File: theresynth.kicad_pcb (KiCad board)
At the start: 2 copper layers, 216 x 69.7 mm, 133 parts, among them J1 Jack-12V AC, J2 AudioJack2, J3 AudioJack2, J4 AudioJack2, J5 AudioJack2, Q1 2N3904, Q2 2N3904, Q3 2N3904, Q4 2N3904, Q5 2N3904, Q6 J111, Q7 2N3904, U1 TL074, U2 LM78L12_TO92, U3 LM79L12_TO92, U4 TL074, U5 TL072

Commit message: completely connected
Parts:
- removed the C38 at (91.3, 100.5)
- removed the D6 at (130.0, 125.5)
- removed the R40 at (77.3, 95.3)
- removed the R42 at (69.7, 90.2)
- removed the R48 at (90.1, 97.7)
- removed the R50 at (90.1, 87.7)
- removed R52, R53: 10k, Resistor_THT:R_Axial_DIN0204_L3.6mm_D1.6mm_P7.62mm_Horizontal
- removed R55: 1k, Resistor_THT:R_Axial_DIN0204_L3.6mm_D1.6mm_P7.62mm_Horizontal
- removed the RV6 at (114.4, 125.5)
- removed the U5 at (90.1, 107.3)
- added ?: , MountingHole:MountingHole_3mm, F.Cu at (48.0, 63.8)
- added ?: , MountingHole:MountingHole_3mm, F.Cu at (254.0, 63.8)
- added ?: , MountingHole:MountingHole_3mm, F.Cu at (254.0, 125.5)
- added ?: , MountingHole:MountingHole_3mm, F.Cu at (48.0, 125.5)
- added C19: 100n, Capacitor_THT:C_Rect_L7.2mm_W2.5mm_P5.00mm_FKS2_FKP2_MKS2_MKP2, F.Cu at (137.4, 95.4)
- added C20: 100n, Capacitor_THT:C_Rect_L7.2mm_W2.5mm_P5.00mm_FKS2_FKP2_MKS2_MKP2, F.Cu at (152.9, 95.4)
- added C39: 100n, Capacitor_THT:C_Rect_L7.2mm_W2.5mm_P5.00mm_FKS2_FKP2_MKS2_MKP2, F.Cu at (78.2, 95.3)
- added C40: 100n, Capacitor_THT:C_Rect_L7.2mm_W2.5mm_P5.00mm_FKS2_FKP2_MKS2_MKP2, F.Cu at (93.6, 94.9)
- added C42: 100n, Capacitor_THT:C_Rect_L7.2mm_W2.5mm_P5.00mm_FKS2_FKP2_MKS2_MKP2, F.Cu at (176.6, 71.0)
- added C43: 100n, Capacitor_THT:C_Rect_L7.2mm_W2.5mm_P5.00mm_FKS2_FKP2_MKS2_MKP2, F.Cu at (192.6, 71.1)
- added D1: LED, LED_THT:LED_D3.0mm, F.Cu at (152.2, 125.8)
- added D7: LED, LED_THT:LED_D3.0mm, F.Cu at (54.2, 125.8)
- added R32: 1k, Resistor_THT:R_Axial_DIN0204_L3.6mm_D1.6mm_P7.62mm_Horizontal, F.Cu at (198.8, 76.2)
- added R34: 5k, Resistor_THT:R_Axial_DIN0204_L3.6mm_D1.6mm_P7.62mm_Horizontal, F.Cu at (198.9, 66.0)
- added R35: 10k, Resistor_THT:R_Axial_DIN0204_L3.6mm_D1.6mm_P7.62mm_Horizontal, F.Cu at (191.3, 63.5)
- added RV4: 100k, Potentiometer_THT:Potentiometer_Bourns_3296W_Vertical, F.Cu at (160.3, 68.3)
- added RV7: 100k, Potentiometer_THT:Potentiometer_Alps_RK163_Single_Horizontal, F.Cu at (72.1, 125.2)
- added SW1: SW_SPST, Eurorack:Horizontal_SPDT_2MS5T2B2M7RE, F.Cu at (61.5, 120.8)
- added U2: TL074, Package_DIP:DIP-14_W7.62mm_LongPads, F.Cu at (180.8, 63.5)
- C3: footprint Capacitor_THT:C_Rect_L7.0mm_W6.5mm_P5.00mm -> Eurorack:Variable_Capacitor_W6.5mm_P5.00mm
- C31: renamed from C29; footprint Capacitor_THT:C_Rect_L7.0mm_W6.5mm_P5.00mm -> Eurorack:Variable_Capacitor_W6.5mm_P5.00mm
- C38: renamed from C36; value 33n -> 100n
- J5: value AudioJack2 -> External Ground; footprint Eurorack:PJ302M -> Connector_Pin:Pin_D1.4mm_L8.5mm_W2.8mm_FlatFork
- R44: renamed from R45; value 100k -> 220k
- R47: renamed from R43; value 100k -> 5k
- R48: renamed from R44; value 100k -> 10k
- R51: value 10k -> 1k
- RV3: value R_POT -> 100k
- RV5: renamed from RV4; footprint Potentiometer_THT:Potentiometer_Alps_RK163_Single_Horizontal -> Potentiometer_THT:Potentiometer_Bourns_3296W_Vertical
- moved R49 83.8 mm to (170.5, 63.5)
- moved R50 76.8 mm to (170.5, 78.8), turned to 0 degrees
- moved R51 67.1 mm to (56.7, 120.2)
- moved R33 38.0 mm to (191.3, 68.5)
- moved R37 36.8 mm to (170.5, 76.2)
- moved J2 33.7 mm to (211.6, 67.7)
- moved R24 32.4 mm to (100.1, 90.1)
- moved R48 30.7 mm to (100.1, 92.3), turned to 180 degrees
- moved R36 20.9 mm to (198.8, 78.8)
- moved RV5 19.7 mm to (78.1, 107.0), turned to 0 degrees
- moved D6 13.4 mm to (119.5, 125.8)
- moved R47 10.8 mm to (92.4, 100.8)
- moved J1 8.21 mm to (80.2, 73.8)
- moved R23 7.90 mm to (151.8, 87.4)
- moved RV6 7.75 mm to (97.8, 125.2)
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- renumbered C19 to C21, C20 to C22, C25 to C23, C21 to C24, C22 to C25, C23 to C26, C24 to C27, C26 to C28, C27 to C29, C28 to C30, C30 to C32, C31 to C33, C32 to C34, C33 to C35, C34 to C36, C35 to C37, C37 to C41, D1 to D2, D2 to D3, D3 to D4, D4 to D5, D5 to D6, J3 to J2, J2 to J3, R30 to R27, R27 to R28, R28 to R29, R29 to R30, R32 to R33, R34 to R36, R33 to R37, R35 to R38, R36 to R39, R37 to R40, R38 to R41, R39 to R42, R41 to R43, R46 to R45, R47 to R46, R54 to R49, R49 to R50, RV5 to RV6, U2 to U3, U3 to U4, U4 to U5
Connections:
- C23 pad 1: Net-(C25-Pad1) -> Net-(C23-Pad1)
- C28 pad 1: Net-(C26-Pad1) (its old number) -> Net-(C28-Pad1)
- C41 pad 1: Net-(C37-Pad1) (its old number) -> Net-(C41-Pad1)
- D2 pad 2: Net-(D1-Pad2) -> Net-(D2-Pad2)
- D3 pad 1: Net-(D1-Pad2) -> Net-(D2-Pad2)
- D4 pad 1: Net-(C25-Pad1) -> Net-(C23-Pad1)
- J1 pad 1: Net-(D1-Pad2) -> Net-(J1-Pad1)
- J4 pad T: VolumeControlOut -> Net-(J4-PadT)
- R33 pad 1: Net-(C25-Pad1) -> Net-(C23-Pad1)
- R36 pad 2: Net-(C26-Pad1) (its old number) -> Net-(C28-Pad1)
- R37 pad 2: Net-(C25-Pad1) -> Net-(R35-Pad1)
- R43 pad 1: Net-(R41-Pad1) -> Net-(R43-Pad1)
- R46 pad 1: Net-(C38-Pad2) -> Net-(C41-Pad1)
- R47 pad 1: Net-(R41-Pad1) -> Net-(R47-Pad1)
- R48 pad 1: Net-(R40-Pad2) -> Net-(R47-Pad1)
- R48 pad 2: Net-(R44-Pad2) -> Net-(R48-Pad2)
- R50 pad 1: VolumeControlOut -> Net-(J4-PadT)
- R50 pad 2: Net-(C38-Pad1) (its old number) -> Net-(R50-Pad2)
- R51 pad 1: Net-(J5-PadT) -> Net-(D7-Pad2)
- R51 pad 2: Net-(R50-Pad1) -> +12V
- RV5 pad 1: +12V -> -12V
- RV5 pad 2: Net-(R42-Pad2) -> Net-(R43-Pad1)
- RV5 pad 3: GND -> +12V
- U1 pad 12: Net-(R26-Pad1) -> Net-(C28-Pad1)
- U1 pad 8: Net-(C26-Pad1) (its old number) -> Net-(C28-Pad1)
- U1 pad 9: Net-(C26-Pad1) (its old number) -> Net-(C28-Pad1)
- U5 pad 10: Net-(C37-Pad1) (its old number) -> Net-(C41-Pad1)
- U5 pad 12: Net-(C38-Pad1) (its old number) -> Net-(R48-Pad2)
- U5 pad 13: Net-(RV6-Pad2) -> VolumeControlOut
- U5 pad 14: Net-(R50-Pad1) -> VolumeControlOut
- U5 pad 2: Net-(R40-Pad2) -> Net-(R44-Pad2)
- U5 pad 3: Net-(R41-Pad1) -> Net-(R43-Pad1)
- U5 pad 8: Net-(C38-Pad1) (its old number) -> Net-(R48-Pad2)
- U5 pad 9: Net-(C38-Pad1) (its old number) -> Net-(R47-Pad1)
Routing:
- net +12V: track 58.8 -> 411.7 mm
- net -12V: track 0.00 -> 287.9 mm
- net Net-(R48-Pad2): track 0.00 -> 119.8 mm
- net Net-(D1-Pad1): track 0.00 -> 99.2 mm
- net Net-(D6-Pad1): track 0.00 -> 95.1 mm
- net Net-(D2-Pad2): track 0.00 -> 71.3 mm
- net Net-(C28-Pad1): track 0.00 -> 69.7 mm
- net Net-(R21-Pad1): track 0.00 -> 65.3 mm
- net Net-(J1-Pad1): track 0.00 -> 60.9 mm
- net Net-(C13-Pad2): track 11.0 -> 66.7 mm
- net Net-(C21-Pad2): track 0.00 -> 53.3 mm
- net Net-(C23-Pad1): track 0.00 -> 53.2 mm
- net Net-(C37-Pad1): track 16.1 -> 65.6 mm
- net Net-(C41-Pad1): track 0.00 -> 49.1 mm
- net Net-(Q5-Pad2): track 7.81 -> 56.8 mm
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- added copper zone on B.Cu, net GND
- added copper zone on F.Cu, net GND
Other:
- board size 216 x 69.7 mm -> 214 x 69.7 mm
- net class Power added: clearance 0.4, trace_width 0.5, via_dia 0.8, via_drill 0.4
- board text added: "Audio Filter"
- board text added: "External Ground"
- board text added: "Fine CV1 Offset"
- board text added: "On/Off"
- board text added: "Pitch Antenna"
- board text added: "Theresynth © 2020 Marco Martin"
- board text added: "V1.0"
- board text added: "Volume Antenna"
- board text added: "Volume CV Offset and Amplifier"
- board text added: "Volume Oscillator"
- board text removed: "Gate Threshold"
- board text removed: "Gate1"

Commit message: add phones output
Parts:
- added J6: AudioJack3_Switch, Connector_Audio:Jack_3.5mm_Ledino_KB3SPRS_Horizontal, F.Cu at (58.8, 153.1)
- added R52: 1k, Resistor_THT:R_Axial_DIN0204_L3.6mm_D1.6mm_P7.62mm_Horizontal, F.Cu at (50.0, 142.7)
- added RV8: 100k, Potentiometer_THT:Potentiometer_Alps_RK163_Single_Horizontal, F.Cu at (25.2, 151.9)
- C24, C25: value 2200u -> 4700u
- C32: value 22p -> 47p
- J5: value External Ground -> Ext. GND
- U3: value LM78L12_TO92 -> LM7812_TO220; footprint Package_TO_SOT_THT:TO-92_Inline_Wide -> Package_TO_SOT_THT:TO-220-3_Vertical
- U4: value LM79L12_TO92 -> LM7912_TO220; footprint Package_TO_SOT_THT:TO-92_Inline_Wide -> Package_TO_SOT_THT:TO-220-3_Vertical
- moved D4 72.9 mm to (215.8, 65.1), turned to 180 degrees
- moved C23 67.3 mm to (213.3, 69.9), turned to 180 degrees
- moved R27 53.2 mm to (205.8, 65.1), turned to 180 degrees
- moved J3 50.6 mm to (186.9, 67.7)
- moved C30 46.3 mm to (106.2, 81.6)
- moved C22 41.7 mm to (200.4, 68.0), turned to 0 degrees
- moved RV4 39.0 mm to (199.1, 72.5), turned to 180 degrees
- moved U3 33.8 mm to (120.8, 78.3)
- moved C29 31.0 mm to (127.2, 81.6), turned to 180 degrees
- moved D2 28.6 mm to (64.5, 82.0), turned to 90 degrees
- moved J5 27.1 mm to (85.2, 63.5)
- moved U4 26.9 mm to (104.8, 78.3)
- moved J1 23.7 mm to (56.5, 73.8)
- moved C42 21.5 mm to (155.1, 71.0)
- moved C43 21.5 mm to (171.1, 71.1)
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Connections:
- R48 pad 2: Net-(R48-Pad2) -> VolumeControlOut
- U1 pad 12: Net-(C28-Pad1) -> Net-(R23-Pad1)
- U2 pad 3: Net-(R48-Pad2) -> VolumeControlOut
- U2 pad 5: Net-(R48-Pad2) -> VolumeControlOut
- U3 pad 1: +12V -> Net-(C24-Pad1)
- U3 pad 3: Net-(C24-Pad1) -> +12V
- U5 pad 12: Net-(R48-Pad2) -> Net-(C28-Pad1)
- U5 pad 13: VolumeControlOut -> Net-(R52-Pad2)
- U5 pad 14: VolumeControlOut -> Net-(R52-Pad2)
- U5 pad 8: Net-(R48-Pad2) -> VolumeControlOut
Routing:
- net -12V: track 287.9 -> 122.6 mm
- net +12V: track 411.7 -> 281.6 mm
- net Net-(R48-Pad2): track 119.8 -> 0.00 mm
- net Net-(D2-Pad2): track 71.3 -> 0.00 mm
- net VolumeControlOut: track 5.26 -> 68.7 mm
- net Net-(J1-Pad1): track 60.9 -> 0.00 mm
- net Net-(J4-PadT): track 47.8 -> 0.00 mm
- net Net-(D6-Pad1): track 95.1 -> 57.0 mm
- net Net-(J3-PadT): track 36.5 -> 0.00 mm
- net Net-(J2-PadT): track 14.7 -> 50.9 mm
- net Net-(C25-Pad2): track 34.2 -> 0.00 mm
- net Net-(C23-Pad1): track 53.2 -> 21.5 mm
- net Net-(C28-Pad1): track 69.7 -> 41.4 mm
- net Net-(C24-Pad1): track 28.0 -> 0.00 mm
- net Net-(D1-Pad1): track 99.2 -> 119.9 mm
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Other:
- board text added: "Ext. GND"
- board text added: "TODO: un jack per parte, l'envelope va spostata tra i due CV"
- board text removed: "External Ground"

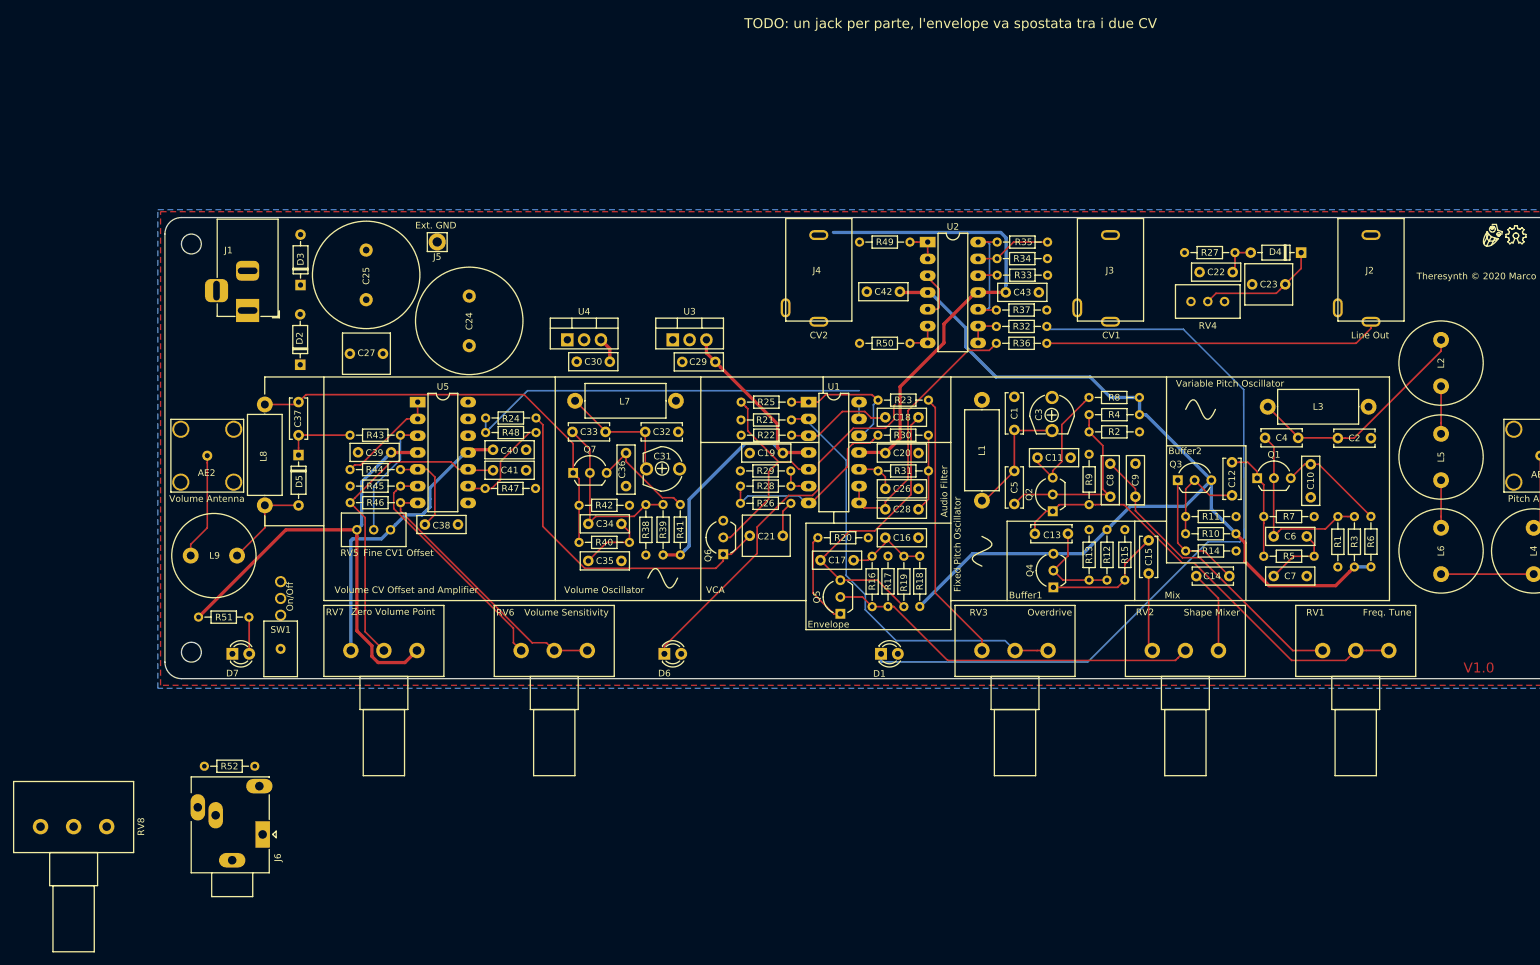
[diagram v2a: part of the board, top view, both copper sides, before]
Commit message: removed 2 opamp units
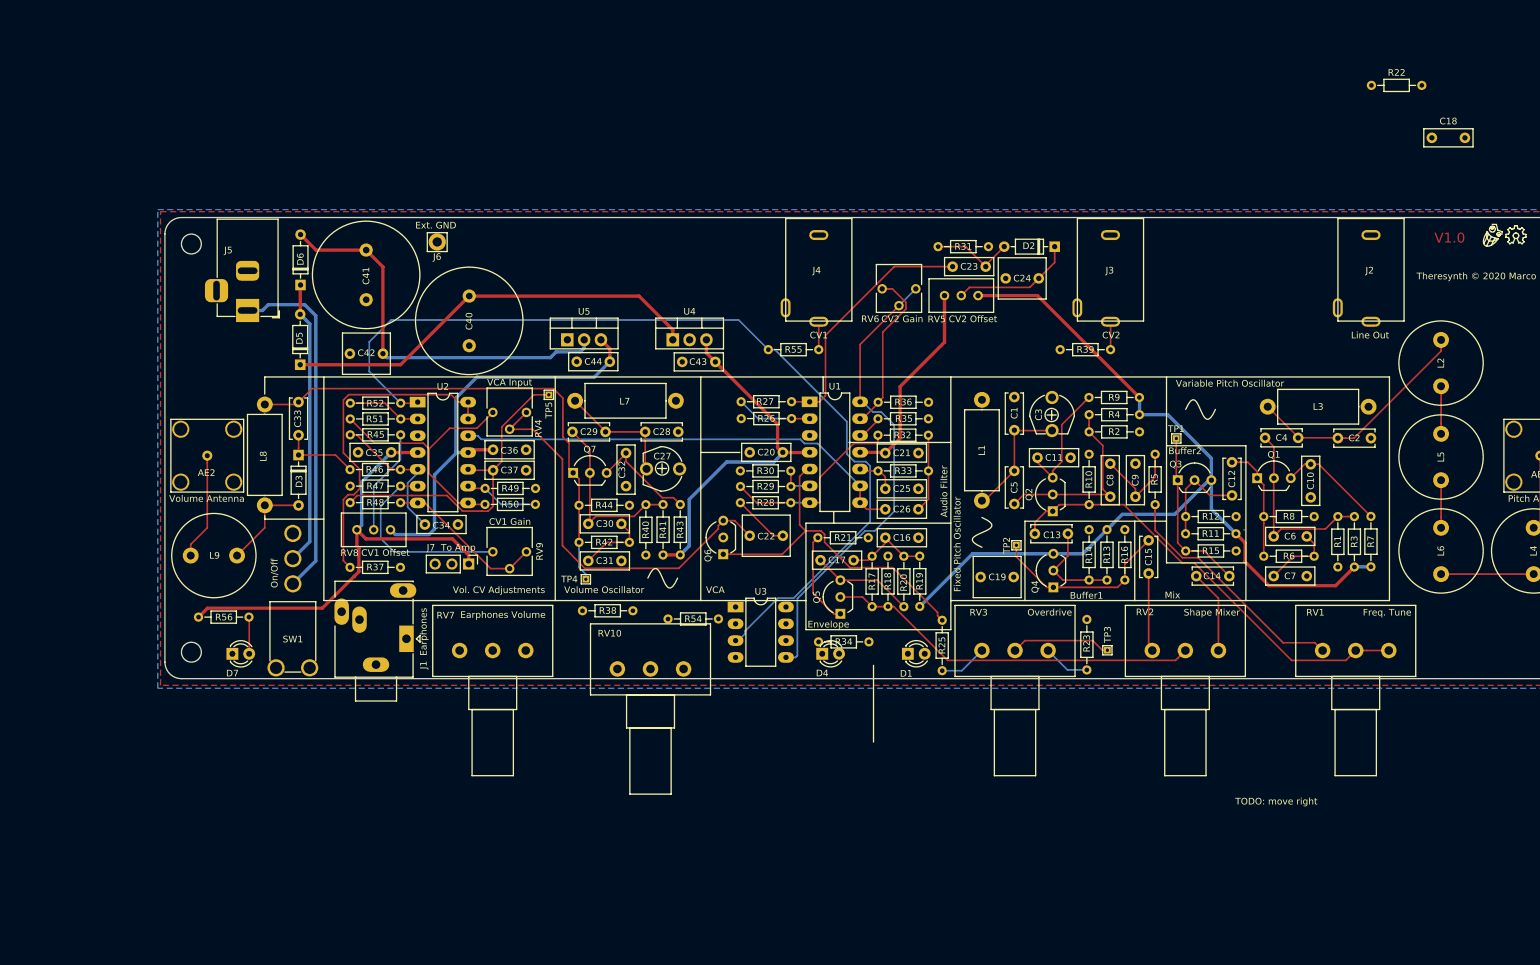
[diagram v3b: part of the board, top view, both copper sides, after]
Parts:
- removed the C42 at (155.1, 71.0)
- removed the C43 at (171.1, 71.1)
- removed the R23 at (151.8, 87.4)
- removed R24: 9.52k, Resistor_THT:R_Axial_DIN0204_L3.6mm_D1.6mm_P7.62mm_Horizontal
- removed the R43 at (79.6, 92.7)
- removed the RV7 at (72.1, 125.2)
- added C18: 10n, Capacitor_THT:C_Rect_L7.2mm_W2.5mm_P5.00mm_FKS2_FKP2_MKS2_MKP2, F.Cu at (235.5, 47.8)
- added J7: To_Amp, Connector_PinHeader_2.54mm:PinHeader_1x03_P2.54mm_Vertical, F.Cu at (89.9, 112.2)
- added R22: 2.2k, Resistor_THT:R_Axial_DIN0204_L3.6mm_D1.6mm_P7.62mm_Horizontal, F.Cu at (226.4, 39.8)
- added R45: 220k, Resistor_THT:R_Axial_DIN0204_L3.6mm_D1.6mm_P7.62mm_Horizontal, F.Cu at (72.0, 92.7)
- added R5: 220, Resistor_THT:R_Axial_DIN0204_L3.6mm_D1.6mm_P7.62mm_Horizontal, F.Cu at (193.7, 103.2)
- added R51: 10k, Resistor_THT:R_Axial_DIN0204_L3.6mm_D1.6mm_P7.62mm_Horizontal, F.Cu at (79.6, 90.2)
- added R52: 10k, Resistor_THT:R_Axial_DIN0204_L3.6mm_D1.6mm_P7.62mm_Horizontal, F.Cu at (72.0, 87.9)
- added RV10: 100k, Potentiometer_THT:Potentiometer_Alps_RK163_Single_Horizontal, F.Cu at (112.4, 128.0)
- added RV4: 10k, Potentiometer_THT:Potentiometer_Vishay_T73YP_Vertical, F.Cu at (93.6, 89.3)
- added RV6: 10k, Potentiometer_THT:Potentiometer_Vishay_T73YP_Vertical, F.Cu at (152.4, 70.6)
- added TP1: TestPoint, TestPoint:TestPoint_THTPad_1.0x1.0mm_Drill0.5mm, F.Cu at (196.9, 93.2)
- added TP2: TestPoint, TestPoint:TestPoint_THTPad_1.0x1.0mm_Drill0.5mm, F.Cu at (172.7, 109.3)
- added TP3: TestPoint, TestPoint:TestPoint_THTPad_1.0x1.0mm_Drill0.5mm, F.Cu at (186.5, 125.2)
- added TP4: TestPoint, TestPoint:TestPoint_THTPad_1.0x1.0mm_Drill0.5mm, F.Cu at (107.6, 114.5)
- added TP5: TestPoint, TestPoint:TestPoint_THTPad_1.0x1.0mm_Drill0.5mm, F.Cu at (102.0, 86.6)
- C1: value 33p -> 22p
- C19: renamed from C18; value 100n -> 1u; footprint Capacitor_THT:C_Rect_L7.2mm_W2.5mm_P5.00mm_FKS2_FKP2_MKS2_MKP2 -> Capacitor_THT:C_Rect_L7.0mm_W6.0mm_P5.00mm
- C2: value 47p -> 22p
- C23: renamed from C22; value 40n -> 10n
- C3: value 60p -> 20p
- Q6: value J111 -> J113
- R23: renamed from R21; value 1k -> 10k
- R26: renamed from R22; value 100k -> 10k
- R27: renamed from R35; value 10k -> 100k
- R31: renamed from R27; value 10k -> 100k
- R36: renamed from R34; value 5k -> 1k
- R49: renamed from R47; value 5k -> 10k
- RV9: renamed from RV6; footprint Potentiometer_THT:Potentiometer_Alps_RK163_Single_Horizontal -> Potentiometer_THT:Potentiometer_Vishay_T73YP_Vertical
- SW1: footprint Eurorack:Horizontal_SPDT_2MS5T2B2M7RE -> Eurorack:Horizontal_SPDT
- U3: renamed from U2; value TL074 -> TL072; footprint Package_DIP:DIP-14_W7.62mm_LongPads -> Package_DIP:DIP-8_W7.62mm_LongPads
- moved R38 74.5 mm to (114.7, 119.2)
- moved RV7 68.7 mm to (88.5, 125.2)
- moved R54 63.9 mm to (120.0, 120.5)
- moved U3 62.3 mm to (130.3, 118.7)
- moved R23 58.5 mm to (183.4, 128.2), turned to 90 degrees
- moved R34 54.7 mm to (150.4, 123.9)
- moved R25 44.8 mm to (161.5, 120.7), turned to 270 degrees
- moved R37 42.2 mm to (79.6, 112.7), turned to 180 degrees
- moved R27 39.3 mm to (138.7, 87.6), turned to 180 degrees
- moved C24 37.3 mm to (176.1, 69.0)
- moved D2 37.3 mm to (178.5, 64.2)
- moved R31 37.3 mm to (168.5, 64.2)
- moved RV5 37.3 mm to (161.8, 71.6)
- moved J1 36.7 mm to (80.5, 123.5)
- moved C23 32.3 mm to (168.1, 67.2), turned to 180 degrees
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- renumbered C19 to C20, C20 to C21, C21 to C22, C23 to C24, C26 to C25, C28 to C26, C31 to C27, C32 to C28, C33 to C29, C34 to C30, C35 to C31, C36 to C32, C37 to C33, C38 to C34, C39 to C35, C40 to C36, C41 to C37, C24 to C40, C25 to C41, C27 to C42, C29 to C43, C30 to C44, D4 to D2, D5 to D3, D6 to D4, D2 to D5, D3 to D6, J6 to J1, J1 to J5, J5 to J6, R9 to R10, R10 to R11, R11 to R12, R12 to R13, R13 to R14, R14 to R15, R15 to R16, R16 to R17, R17 to R18, R18 to R19, R19 to R20, R20 to R21, R26 to R28, R28 to R29, R29 to R30, R30 to R32, R31 to R33, R32 to R34, R33 to R35, R52 to R37, R36 to R38, R37 to R39, R38 to R40, R39 to R41, R40 to R42, R41 to R43, R42 to R44, R44 to R46, R45 to R47, R46 to R48, R48 to R50, R49 to R54, R50 to R55, R51 to R56, R5 to R6, R6 to R7, R7 to R8, R8 to R9, RV4 to RV5, RV8 to RV7, RV5 to RV8, U5 to U2, U3 to U4, U4 to U5
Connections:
- C19 pad 1: Net-(C18-Pad1) -> Net-(C19-Pad1)
- C19 pad 2: Net-(C17-Pad2) -> Net-(C18-Pad1)
- C22 pad 2: Net-(C21-Pad2) -> Net-(C22-Pad2)
- C23 pad 1: GND -> Net-(C23-Pad1)
- C23 pad 2: Net-(C22-Pad2) -> Net-(C23-Pad2)
- C24 pad 1: Net-(C23-Pad1) -> Net-(C24-Pad1)
- C33 pad 2: Net-(C37-Pad2) -> Net-(C33-Pad2)
- D2 pad 1: Net-(C23-Pad1) -> Net-(C24-Pad1)
- D2 pad 2: Net-(C22-Pad2) -> Net-(C23-Pad1)
- D3 pad 1: Net-(C37-Pad2) -> Net-(C33-Pad2)
- D4 pad 1: Net-(D6-Pad1) -> GND
- D4 pad 2: GND -> Net-(D4-Pad2)
- J1 pad TN: (no net) -> Net-(J1-PadTN)
- Q6 pad 1: Net-(C21-Pad2) -> Net-(Q6-Pad1)
- Q6 pad 2: Net-(Q6-Pad2) -> GND
- Q6 pad 3: GND -> Net-(C22-Pad2)
- R23 pad 1: Net-(R21-Pad1) -> Net-(R23-Pad1)
- R25 pad 1: Net-(Q6-Pad2) -> Net-(Q6-Pad1)
- R25 pad 2: Net-(R23-Pad1) -> Net-(R25-Pad2)
- R26 pad 2: Net-(C18-Pad1) -> Net-(R26-Pad2)
- R27 pad 1: Net-(R35-Pad1) -> Net-(C23-Pad2)
- R27 pad 2: Net-(R34-Pad2) -> Net-(R26-Pad2)
- R31 pad 1: Net-(C22-Pad2) -> GND
- R31 pad 2: Net-(R27-Pad2) -> Net-(C23-Pad1)
- R34 pad 2: Net-(R32-Pad2) -> Net-(R34-Pad2)
- R35 pad 1: Net-(C23-Pad1) -> Net-(C24-Pad1)
- R36 pad 2: Net-(R34-Pad2) -> Net-(R36-Pad2)
- R38 pad 1: Net-(J2-PadT) -> Net-(R38-Pad1)
- R39 pad 2: Net-(R35-Pad1) -> Net-(R39-Pad2)
- R46 pad 2: Net-(R44-Pad2) -> Net-(C33-Pad2)
- R54 pad 1: Net-(D6-Pad1) -> Net-(D4-Pad2)
- R55 pad 2: Net-(R50-Pad2) -> Net-(R52-Pad2)
- RV1 pad 1: Net-(C8-Pad2) -> Net-(R5-Pad1)
- RV3 pad 1: Net-(R23-Pad2) -> Net-(R25-Pad2)
- RV3 pad 2: Net-(R21-Pad1) -> Net-(C19-Pad1)
- RV3 pad 3: Net-(R21-Pad1) -> Net-(R23-Pad1)
- RV5 pad 2: Net-(C23-Pad1) -> Net-(C24-Pad1)
- RV8 pad 2: Net-(R43-Pad1) -> Net-(R45-Pad2)
- U1 pad 1: Net-(R23-Pad1) -> Net-(C23-Pad2)
- U1 pad 12: Net-(R23-Pad1) -> Net-(C24-Pad1)
- U1 pad 13: Net-(R27-Pad2) -> Net-(R36-Pad2)
- U1 pad 14: Net-(R27-Pad2) -> Net-(R39-Pad2)
- U1 pad 2: Net-(R21-Pad1) -> Net-(R26-Pad2)
- U1 pad 3: Net-(C18-Pad1) -> Net-(C19-Pad1)
- U1 pad 5: Net-(Q6-Pad2) -> Net-(Q6-Pad1)
- U2 pad 1: Net-(R44-Pad2) -> Net-(R52-Pad2)
- U2 pad 2: Net-(R44-Pad2) -> Net-(R51-Pad1)
- U2 pad 3: Net-(R43-Pad1) -> GND
- U3 pad 3: VolumeControlOut -> Net-(R52-Pad2)
- U3 pad 4: +12V -> -12V
- U3 pad 5: VolumeControlOut -> Net-(R39-Pad2)
- U3 pad 6: Net-(R50-Pad2) -> Net-(R34-Pad2)
- U3 pad 7: Net-(R50-Pad2) -> Net-(R34-Pad2)
- U3 pad 8: Net-(R32-Pad2) -> +12V
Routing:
- net Net-(R52-Pad2): track 0.00 -> 139.4 mm
- net Net-(D1-Pad1): track 119.9 -> 0.00 mm
- net Net-(R39-Pad2): track 0.00 -> 70.8 mm
- net Net-(R21-Pad1): track 65.3 -> 0.00 mm
- net Net-(C40-Pad1): track 0.00 -> 64.2 mm
- net Net-(C41-Pad2): track 0.00 -> 60.1 mm
- net Net-(D6-Pad1): track 57.0 -> 0.00 mm
- net Net-(C22-Pad2): track 5.47 -> 60.5 mm
- net Net-(C21-Pad2): track 53.3 -> 0.00 mm
- net Net-(J5-Pad1): track 0.00 -> 53.3 mm
- net Net-(Q6-Pad1): track 0.00 -> 51.7 mm
- net Net-(J2-PadT): track 50.9 -> 0.00 mm
- net Net-(R37-Pad2): track 0.24 -> 50.7 mm
- net Net-(D5-Pad2): track 0.00 -> 43.0 mm
- net Net-(R23-Pad2): track 41.1 -> 0.00 mm
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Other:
- board text added: "CV1 Gain"
- board text added: "CV1 Offset"
- board text added: "CV2 Gain"
- board text added: "CV2 Offset"
- board text added: "Earphones"
- board text added: "Earphones Volume"
- board text added: "TODO: move right"
- board text added: "To Amp"
- board text added: "VCA Input"
- board text added: "Vol. CV Adjustments"
- board text removed: "Fine CV1 Offset"
- board text removed: "TODO: un jack per parte, l'envelope va spostata tra i due CV"
- board text removed: "Volume CV Offset and Amplifier"
- board text removed: "Volume Sensitivity"
- board text removed: "Zero Volume Point"
